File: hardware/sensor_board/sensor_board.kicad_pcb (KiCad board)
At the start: 2 copper layers, 65 x 140 mm, 88 parts, among them IC1 ATMEGA88A-A, J1 RJ45_8P8C_8FACH, K1 pow_sel, P1 UART, P2 Shield, P3 i2c_pow, P4 i2c_chain, P5 12Vin, P6 HOHLBUCHSE, P7 Vccin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

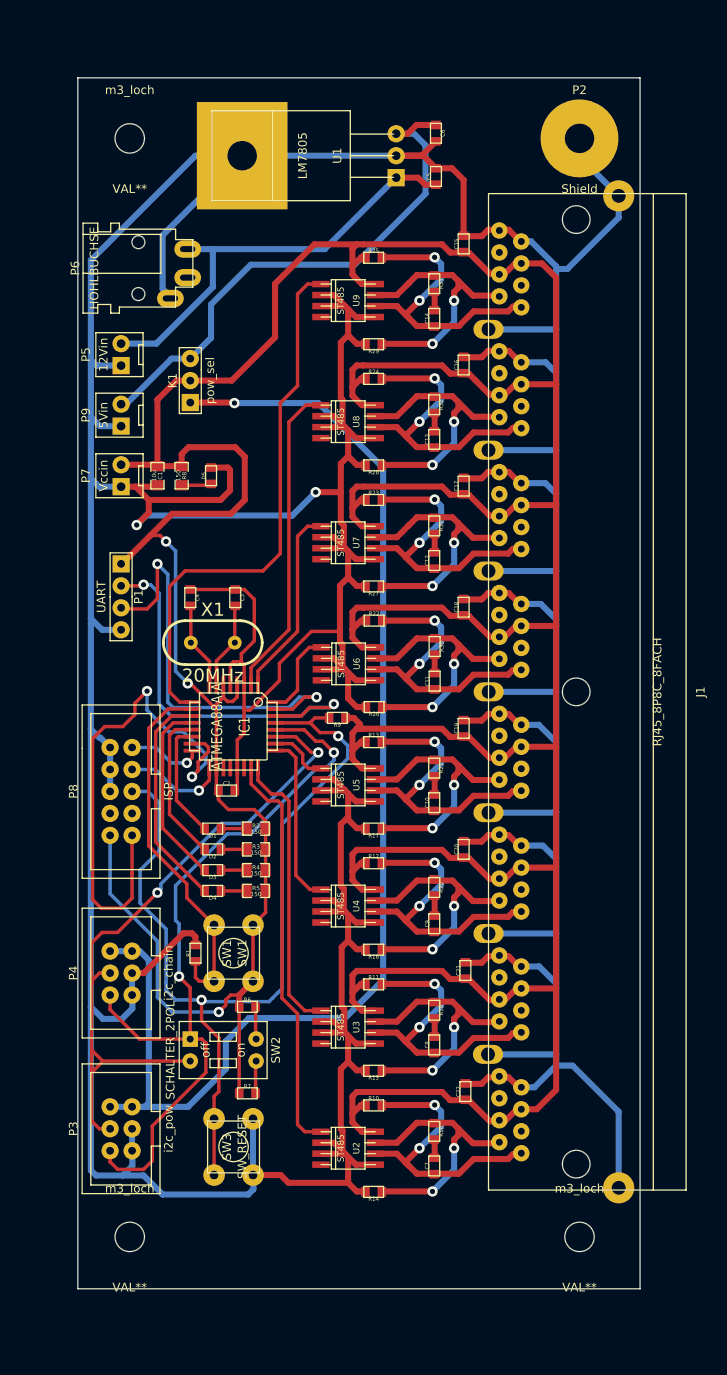
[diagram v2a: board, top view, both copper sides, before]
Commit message: zones added
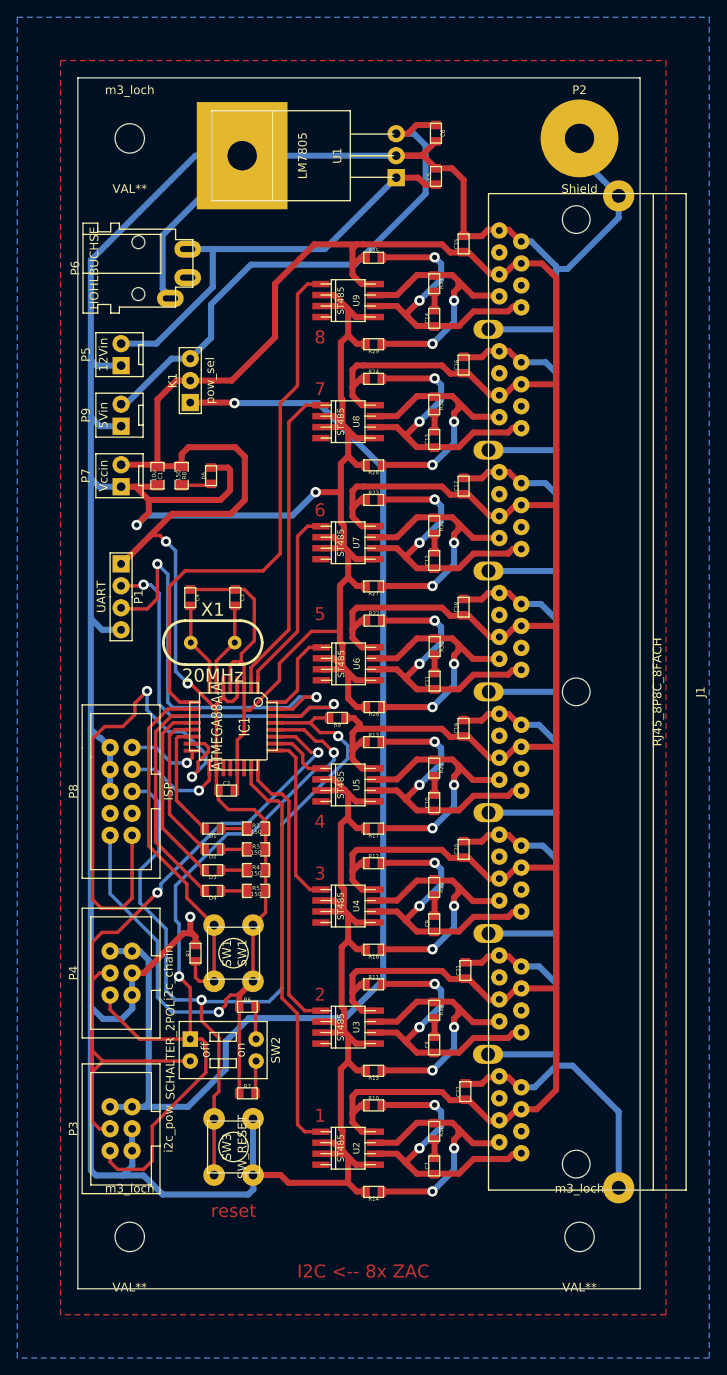
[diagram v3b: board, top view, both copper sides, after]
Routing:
- net GND: track 854.1 -> 856.0 mm, vias 2 -> 3
- added copper zone on B.Cu, net GND
- added copper zone on F.Cu, net GND
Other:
- board text added: "1"
- board text added: "2"
- board text added: "3"
- board text added: "4"
- board text added: "5"
- board text added: "6"
- board text added: "7"
- board text added: "8"
- board text added: "I2C <-- 8x ZAC"
- board text added: "reset"
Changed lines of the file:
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@@
     (links 256)
     (no_connects 0)
-    (area 195.671 34.150001 281.714285 182.671)
+    (area 190 34.150001 281.714285 190.000001)
     (thickness 1.6)
-    (drawings 6)
-    (tracks 1142)
+    (drawings 16)
+    (tracks 1145)
     (zones 0)
     (modules 88)
@@
       (outputformat 1)
       (mirror false)
-      (drillshape 1)
+      (drillshape 0)
       (scaleselection 1)
       (outputdirectory ""))
@@
     )
   )
+  (gr_text "I2C <-- 8x ZAC" (at 230 180) (layer F.Cu)
+    (effects (font (size 1.5 1.5) (thickness 0.3)))
+  )
+  (gr_text reset (at 215 173) (layer F.Cu)
+    (effects (font (size 1.5 1.5) (thickness 0.3)))
+  )
+  (gr_text 8 (at 225 72) (layer F.Cu)
+    (effects (font (size 1.5 1.5) (thickness 0.3)))
+  )
+  (gr_text 7 (at 225 78) (layer F.Cu)
+    (effects (font (size 1.5 1.5) (thickness 0.3)))
+  )
+  (gr_text 6 (at 225 92) (layer F.Cu)
+    (effects (font (size 1.5 1.5) (thickness 0.3)))
+  )
+  (gr_text 5 (at 225 104) (layer F.Cu)
+    (effects (font (size 1.5 1.5) (thickness 0.3)))
+  )
+  (gr_text 4 (at 225 128) (layer F.Cu)
+    (effects (font (size 1.5 1.5) (thickness 0.3)))
+  )
+  (gr_text 3 (at 225 134) (layer F.Cu)
+    (effects (font (size 1.5 1.5) (thickness 0.3)))
+  )
+  (gr_text 2 (at 225 148) (layer F.Cu)
+    (effects (font (size 1.5 1.5) (thickness 0.3)))
+  )
+  (gr_text 1 (at 225 162) (layer F.Cu)
+    (effects (font (size 1.5 1.5) (thickness 0.3)))
+  )
   (dimension 140 (width 0.3) (layer Cmts.User)
     (gr_text "140.000 mm" (at 274.349999 112 270) (layer Cmts.User)
@@
   (segment (start 241 65.5) (end 242.676 67.176) (width 0.7) (layer F.Cu) (net 42))
   (segment (start 242.676 67.176) (end 245.7296 67.176) (width 0.7) (layer F.Cu) (net 42) (status 20))
+  (segment (start 210 140.9) (end 210 139) (width 0.7) (layer F.Cu) (net 43))
+  (via (at 210 139) (size 1.2) (layers F.Cu B.Cu) (net 43))
   (segment (start 244.4796 126.956) (end 252.3 126.956) (width 0.7) (layer B.Cu) (net 43) (status 400000))
   (segment (start 252.3 126.956) (end 252.3 126.9) (width 0.7) (layer B.Cu) (net 43))
@@
   (segment (start 204.6 145.5) (end 203.27 145.5) (width 0.7) (layer F.Cu) (net 43))
   (segment (start 209.2 140.9) (end 204.6 145.5) (width 0.7) (layer F.Cu) (net 43))
-  (segment (start 210.2 140.9) (end 209.2 140.9) (width 0.7) (layer F.Cu) (net 43))
+  (segment (start 210.2 140.9) (end 210 140.9) (width 0.7) (layer F.Cu) (net 43))
+  (segment (start 210 140.9) (end 209.2 140.9) (width 0.7) (layer F.Cu) (net 43))
   (segment (start 210.6 141.3) (end 210.2 140.9) (width 0.7) (layer F.Cu) (net 43))
   (segment (start 248.2696 144.736) (end 250.336 144.736) (width 0.7) (layer B.Cu) (net 43))
@@
   (segment (start 230.305 104.75) (end 229.75 104.75) (width 0.7) (layer F.Cu) (net 59))
   (segment (start 229.75 104.75) (end 228.75 105.75) (width 0.7) (layer F.Cu) (net 59))
+  (zone (net 43) (net_name GND) (layer F.Cu) (hatch edge 0.508)
+    (connect_pads (clearance 0.508))
+    (min_thickness 0.254)
+    (fill (arc_segments 16) (thermal_gap 0.508) (thermal_bridge_width 0.508))
+    (polygon
+      (pts
+        (xy 265 185) (xy 195 185) (xy 195 40) (xy 265 40)
+      )
+    )
+  )
+  (zone (net 43) (net_name GND) (layer B.Cu) (hatch edge 0.508)
+    (connect_pads (clearance 0.508))
+    (min_thickness 0.254)
+    (fill (arc_segments 16) (thermal_gap 0.508) (thermal_bridge_width 0.508))
+    (polygon
+      (pts
+        (xy 270 190) (xy 190 190) (xy 190 35) (xy 270 35)
+      )
+    )
+  )
 )

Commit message: fixed unconnected zac wire
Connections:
- J1 pad b1: (no net) -> /z2a
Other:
- rule trace_min: 0.254 -> 0.5
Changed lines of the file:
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@@
 (kicad_pcb (version 3) (host pcbnew "(2013-may-18)-stable")
   (general
-    (links 256)
+    (links 257)
     (no_connects 0)
     (area 190 34.150001 281.714285 190.000001)
@@
     (zone_clearance 0.508)
     (zone_45_only no)
-    (trace_min 0.254)
+    (trace_min 0.5)
     (segment_width 0.2)
     (edge_width 0.1)
@@
   (net 49 N-0000024)
   (net 50 N-000004)
-  (net 51 N-0000062)
-  (net 52 N-0000063)
-  (net 53 N-0000064)
-  (net 54 N-0000066)
+  (net 51 N-0000061)
+  (net 52 N-0000062)
+  (net 53 N-0000063)
+  (net 54 N-0000065)
   (net 55 N-000007)
-  (net 56 N-0000085)
-  (net 57 N-0000086)
-  (net 58 N-0000087)
+  (net 56 N-0000084)
+  (net 57 N-0000085)
+  (net 58 N-0000086)
   (net 59 VCC)
   (net_class Default "This is the default net class."
@@
     (add_net /Vreg)
     (add_net GND)
+    (add_net N-0000061)
+    (add_net N-0000065)
+    (add_net N-0000084)
   )
   (net_class uc ""
@@
     (add_net N-0000062)
     (add_net N-0000063)
-    (add_net N-0000064)
-    (add_net N-0000066)
     (add_net N-000007)
     (add_net N-0000085)
     (add_net N-0000086)
-    (add_net N-0000087)
     (add_net VCC)
   )
@@
     (pad 1 smd rect (at -1.108 0) (size 1.2 1.397)
       (layers F.Cu F.Paste F.Mask)
-      (net 51 N-0000062)
+      (net 51 N-0000061)
     )
     (pad 2 smd rect (at 1.108 0) (size 1.2 1.397)
@@
     (pad 2 smd rect (at 1.108 0 270) (size 1.2 1.397)
       (layers F.Cu F.Paste F.Mask)
-      (net 53 N-0000064)
+      (net 53 N-0000063)
     )
     (model smd/chip_cms.wrl
@@
     (pad 1 smd rect (at -1.108 0) (size 1.2 1.397)
       (layers F.Cu F.Paste F.Mask)
-      (net 52 N-0000063)
+      (net 52 N-0000062)
     )
     (pad 2 smd rect (at 1.108 0) (size 1.2 1.397)
@@
     (pad 2 smd rect (at 0.945 0 270) (size 1 1.143)
       (layers F.Cu F.Paste F.Mask)
-      (net 54 N-0000066)
+      (net 54 N-0000065)
     )
     (model smd\resistors\R0603.wrl
@@
     (pad 1 smd rect (at -0.945 0 90) (size 1 1.143)
       (layers F.Cu F.Paste F.Mask)
-      (net 53 N-0000064)
+      (net 53 N-0000063)
     )
     (pad 2 smd rect (at 0.945 0 90) (size 1 1.143)
@@
     (pad 1 smd rect (at -0.945 0 180) (size 1 1.143)
       (layers F.Cu F.Paste F.Mask)
-      (net 52 N-0000063)
+      (net 52 N-0000062)
     )
     (pad 2 smd rect (at 0.945 0 180) (size 1 1.143)
@@
     (pad 1 smd rect (at -0.945 0 180) (size 1 1.143)
       (layers F.Cu F.Paste F.Mask)
-      (net 51 N-0000062)
+      (net 51 N-0000061)
     )
     (pad 2 smd rect (at 0.945 0 180) (size 1 1.143)
@@
     (pad 2 smd rect (at 0.945 0 90) (size 1 1.143)
       (layers F.Cu F.Paste F.Mask)
-      (net 54 N-0000066)
+      (net 54 N-0000065)
     )
     (model smd\resistors\R0603.wrl
@@
     (pad 2 smd rect (at 0.945 0 270) (size 1 1.143)
       (layers F.Cu F.Paste F.Mask)
-      (net 57 N-0000086)
+      (net 57 N-0000085)
     )
     (model smd\resistors\R0603.wrl
@@
     (pad 2 smd rect (at 0.945 0 90) (size 1 1.143)
       (layers F.Cu F.Paste F.Mask)
-      (net 58 N-0000087)
+      (net 58 N-0000086)
     )
     (model smd\resistors\R0603.wrl
@@
     (pad 2 smd rect (at 0.945 0 270) (size 1 1.143)
       (layers F.Cu F.Paste F.Mask)
-      (net 58 N-0000087)
+      (net 58 N-0000086)
     )
     (model smd\resistors\R0603.wrl
@@
     (pad 2 smd rect (at 0.945 0 90) (size 1 1.143)
       (layers F.Cu F.Paste F.Mask)
-      (net 56 N-0000085)
+      (net 56 N-0000084)
     )
     (model smd\resistors\R0603.wrl
@@
     (pad 2 smd rect (at 0.945 0 270) (size 1 1.143)
       (layers F.Cu F.Paste F.Mask)
-      (net 56 N-0000085)
+      (net 56 N-0000084)
     )
     (model smd\resistors\R0603.wrl
@@
     (pad 2 smd rect (at 0.945 0 90) (size 1 1.143)
       (layers F.Cu F.Paste F.Mask)
-      (net 57 N-0000086)
+      (net 57 N-0000085)
     )
     (model smd\resistors\R0603.wrl
@@
     (pad b1 thru_hole circle (at -39.356 -10.7304 90) (size 1.9 1.9) (drill 0.8)
       (layers *.Cu *.Mask F.SilkS)
+      (net 29 /z2a)
     )
     (pad a8 thru_hole circle (at -44.436 -13.2704 90) (size 1.9 1.9) (drill 0.8)
@@
   (segment (start 206.2 102.2) (end 205 103.4) (width 0.4) (layer F.Cu) (net 14))
   (segment (start 206.2 100.2) (end 206.2 102.2) (width 0.4) (layer F.Cu) (net 14))
-  (segment (start 203.27 142.96) (end 204.16 142.96) (width 0.7) (layer B.Cu) (net 15) (status C00000))
+  (segment (start 203.27 142.96) (end 204.16 142.96) (width 0.7) (layer B.Cu) (net 15))
   (segment (start 205.2 160.5) (end 204.74 160.96) (width 0.7) (layer B.Cu) (net 15))
   (segment (start 205.2 144) (end 205.2 160.5) (width 0.7) (layer B.Cu) (net 15))
-  (segment (start 204.16 142.96) (end 205.2 144) (width 0.7) (layer B.Cu) (net 15) (status 400000))
+  (segment (start 204.16 142.96) (end 205.2 144) (width 0.7) (layer B.Cu) (net 15))
   (segment (start 204.54 160.96) (end 204.74 160.96) (width 0.7) (layer B.Cu) (net 15))
   (segment (start 204.54 160.96) (end 203.27 160.96) (width 0.7) (layer B.Cu) (net 15))
@@
   (segment (start 210 140.9) (end 210 139) (width 0.7) (layer F.Cu) (net 43))
   (via (at 210 139) (size 1.2) (layers F.Cu B.Cu) (net 43))
-  (segment (start 244.4796 126.956) (end 252.3 126.956) (width 0.7) (layer B.Cu) (net 43) (status 400000))
+  (segment (start 244.4796 126.956) (end 252.3 126.956) (width 0.7) (layer B.Cu) (net 43))
   (segment (start 252.3 126.956) (end 252.3 126.9) (width 0.7) (layer B.Cu) (net 43))
   (segment (start 252.3 126.9) (end 252.1 126.9) (width 0.7) (layer B.Cu) (net 43))
@@
   (segment (start 210 112) (end 209.7 112) (width 0.4) (layer F.Cu) (net 59))
   (segment (start 212.6 114.6) (end 210 112) (width 0.4) (layer F.Cu) (net 59))
-  (segment (start 200.73 129.58) (end 200.73 136.33) (width 0.4) (layer B.Cu) (net 59) (status 400000))
+  (segment (start 200.73 129.58) (end 200.73 136.33) (width 0.4) (layer B.Cu) (net 59))
   (segment (start 214.65336 148.04664) (end 215.655 148.04664) (width 0.4) (layer F.Cu) (net 59))
   (segment (start 214.1 148.6) (end 214.65336 148.04664) (width 0.4) (layer F.Cu) (net 59))

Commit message: sensor_board complete
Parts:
- added C23: 10u, SM0805_big, F.Cu at (211.4, 88.0)
- added C24: 10u, SM0805_big, F.Cu at (208.8, 88.0)
- added C25: 100n, SM0603_big, F.Cu at (227.6, 63.4)
- added C26: 100n, SM0603_big, F.Cu at (227.8, 75.2)
- added C27: 100n, SM0603_big, F.Cu at (227.9, 89.1)
- added C28: 100n, SM0603_big, F.Cu at (227.9, 103.1)
- added C29: 100n, SM0603_big, F.Cu at (227.7, 119.7)
- added C30: 100n, SM0603_big, F.Cu at (227.9, 131.2)
- added C31: 100n, SM0603_big, F.Cu at (227.9, 145.3)
- added C32: 100n, SM0603_big, F.Cu at (227.7, 159.2)
- added R34: 0, SM0805_big, F.Cu at (245.2, 49.0)
- moved R8 5.00 mm to (214.0, 88.0)
- moved D5 4.00 mm to (216.4, 88.0)
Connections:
- P2 pad 1: GND -> N-0000027
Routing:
- net GND: track 856.0 -> 879.8 mm
- net N-0000027: track 0.00 -> 8.69 mm
- net VCC: track 563.9 -> 556.5 mm
- net N-0000066: track 3.47 -> 2.47 mm
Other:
- rule trace_min: 0.5 -> 0.4
- board text added: "v1.0"

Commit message: sensor_board final version
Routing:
- net /MOSI: track 61.3 -> 49.6 mm
- net GND: track 879.8 -> 884.0 mm
- net +12V: track 50.2 -> 53.8 mm
- net /Vreg: track 62.1 -> 65.1 mm

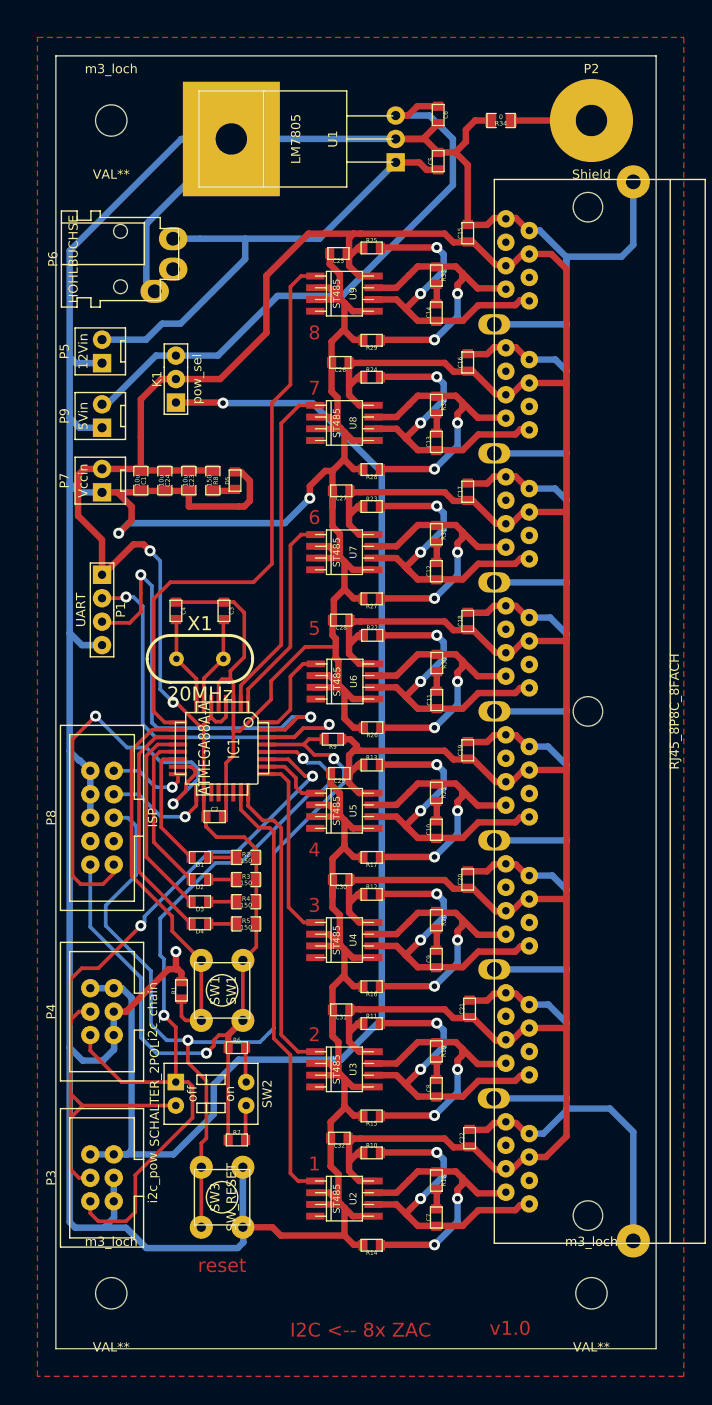
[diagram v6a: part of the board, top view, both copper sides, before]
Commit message: sensor board smaller
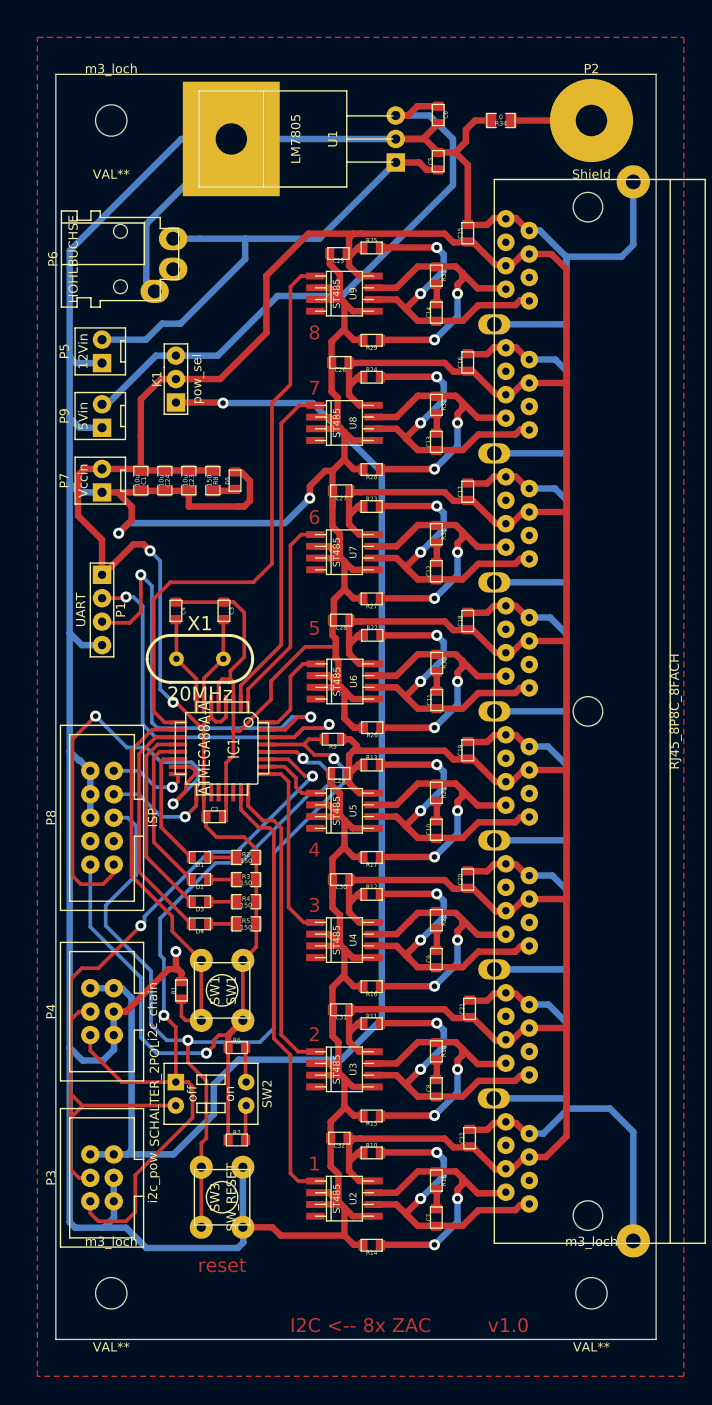
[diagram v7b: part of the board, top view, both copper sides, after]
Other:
- board size 65 x 140 mm -> 65 x 137 mm
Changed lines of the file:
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@@
     (links 278)
     (no_connects 0)
-    (area 196.949999 41.949999 262.050001 182.050001)
+    (area 190 34.150001 281.714285 190.000001)
     (thickness 1.6)
     (drawings 17)
@@
     )
   )
-  (gr_text v1.0 (at 246.2 179.8) (layer F.Cu)
+  (dimension 137 (width 0.3) (layer Cmts.User)
+    (gr_text "137.000 mm" (at 279.85 112.5 90) (layer Cmts.User)
+      (effects (font (size 1.5 1.5) (thickness 0.3)))
+    )
+    (feature1 (pts (xy 263 44) (xy 281.2 44)))
+    (feature2 (pts (xy 263 181) (xy 281.2 181)))
+    (crossbar (pts (xy 278.5 181) (xy 278.5 44)))
+    (arrow1a (pts (xy 278.5 44) (xy 279.08642 45.126503)))
+    (arrow1b (pts (xy 278.5 44) (xy 277.91358 45.126503)))
+    (arrow2a (pts (xy 278.5 181) (xy 279.08642 179.873497)))
+    (arrow2b (pts (xy 278.5 181) (xy 277.91358 179.873497)))
+  )
+  (gr_line (start 197 181) (end 197 44) (angle 90) (layer Edge.Cuts) (width 0.1))
+  (gr_line (start 262 181) (end 197 181) (angle 90) (layer Edge.Cuts) (width 0.1))
+  (gr_line (start 262 44) (end 262 181) (angle 90) (layer Edge.Cuts) (width 0.1))
+  (gr_line (start 197 44) (end 262 44) (angle 90) (layer Edge.Cuts) (width 0.1))
+  (gr_text v1.0 (at 246 179.5) (layer F.Cu)
     (effects (font (size 1.5 1.5) (thickness 0.3)))
   )
-  (gr_text "I2C <-- 8x ZAC" (at 230 180) (layer F.Cu)
+  (gr_text "I2C <-- 8x ZAC" (at 230 179.5) (layer F.Cu)
     (effects (font (size 1.5 1.5) (thickness 0.3)))
   )
@@
     (effects (font (size 1.5 1.5) (thickness 0.3)))
   )
-  (dimension 140 (width 0.3) (layer Cmts.User)
-    (gr_text "140.000 mm" (at 274.349999 112 270) (layer Cmts.User)
-      (effects (font (size 1.5 1.5) (thickness 0.3)))
-    )
-    (feature1 (pts (xy 263 182) (xy 275.699999 182)))
-    (feature2 (pts (xy 263 42) (xy 275.699999 42)))
-    (crossbar (pts (xy 272.999999 42) (xy 272.999999 182)))
-    (arrow1a (pts (xy 272.999999 182) (xy 272.413579 180.873497)))
-    (arrow1b (pts (xy 272.999999 182) (xy 273.586419 180.873497)))
-    (arrow2a (pts (xy 272.999999 42) (xy 272.413579 43.126503)))
-    (arrow2b (pts (xy 272.999999 42) (xy 273.586419 43.126503)))
-  )
   (dimension 65 (width 0.3) (layer Cmts.User)
     (gr_text "65.000 mm" (at 229.5 35.650001) (layer Cmts.User)
@@
     (arrow2b (pts (xy 262 37.000001) (xy 260.873497 37.586421)))
   )
-  (gr_line (start 197 182) (end 197 42) (angle 90) (layer Edge.Cuts) (width 0.1))
-  (gr_line (start 262 182) (end 197 182) (angle 90) (layer Edge.Cuts) (width 0.1))
-  (gr_line (start 262 42) (end 262 182) (angle 90) (layer Edge.Cuts) (width 0.1))
-  (gr_line (start 197 42) (end 262 42) (angle 90) (layer Edge.Cuts) (width 0.1))
-  (segment (start 202 72.73) (end 206.77 72.73) (width 0.7) (layer B.Cu) (net 1) (status 400000))
+  (segment (start 202 72.73) (end 206.77 72.73) (width 0.7) (layer B.Cu) (net 1))
   (segment (start 217.5 64) (end 217.5 61.8) (width 0.7) (layer B.Cu) (net 1))
   (segment (start 210.5 71) (end 217.5 64) (width 0.7) (layer B.Cu) (net 1))
